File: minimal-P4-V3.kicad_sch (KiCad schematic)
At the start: 49 parts, among them U1 TLV62569DBV, U3 W25Q128JVS, Y1 40MHz(+-10 ppm)

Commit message: Start work on layout
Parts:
- C1, C12, C13, C15, C16, C17, C18, C19, C2, C21, C22, C23, C24, C25, C26, C27, C29, C30, C31, C32, C33, C4, C40, C41, C42, C5, C6, C7, C8, C9: footprint (none) -> Capacitor_SMD:C_0402_1005Metric
- C11, C14, C20, C28, C3: footprint (none) -> Capacitor_SMD:C_0603_1608Metric
- L1: footprint (none) -> Inductor_SMD:L_1008_2520Metric
- R1, R2, R200, R209, R210, R28, R3, R39, R4: footprint (none) -> Resistor_SMD:R_0402_1005Metric
- U2: footprint PCM_Espressif:ESP32-P4 -> Espressif:ESP32-P4
- Y1: value 40MHz(+-10 ppm) -> 40MHz(+-10 ppm) C501798; footprint (none) -> Crystal:Crystal_SMD_2016-4Pin_2.0x1.6mm
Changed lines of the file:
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@@
 			)
 		)
-		(property "Footprint" ""
+		(property "Footprint" "Capacitor_SMD:C_0402_1005Metric"
 			(at 140.97 186.69 0)
 			(hide yes)
@@
 			)
 		)
-		(property "Footprint" ""
+		(property "Footprint" "Capacitor_SMD:C_0402_1005Metric"
 			(at 231.14 41.91 0)
 			(hide yes)
@@
 			)
 		)
-		(property "Footprint" ""
+		(property "Footprint" "Capacitor_SMD:C_0402_1005Metric"
 			(at 220.98 71.12 0)
 			(hide yes)
@@
 			)
 		)
-		(property "Footprint" ""
+		(property "Footprint" "Resistor_SMD:R_0402_1005Metric"
 			(at 270.51 115.57 0)
 			(hide yes)
@@
 			)
 		)
-		(property "Footprint" ""
+		(property "Footprint" "Capacitor_SMD:C_0402_1005Metric"
 			(at 140.97 48.26 0)
 			(hide yes)
@@
 			)
 		)
-		(property "Footprint" ""
+		(property "Footprint" "Capacitor_SMD:C_0603_1608Metric"
 			(at 27.94 107.95 0)
 			(hide yes)
@@
 			)
 		)
-		(property "Footprint" ""
+		(property "Footprint" "Capacitor_SMD:C_0402_1005Metric"
 			(at 196.85 71.12 0)
 			(hide yes)
@@
 			)
 		)
-		(property "Footprint" ""
+		(property "Footprint" "Inductor_SMD:L_1008_2520Metric"
 			(at 213.36 39.37 0)
 			(hide yes)
@@
 			)
 		)
-		(property "Footprint" ""
+		(property "Footprint" "Resistor_SMD:R_0402_1005Metric"
 			(at 222.25 41.91 0)
 			(hide yes)
@@
 			)
 		)
-		(property "Footprint" ""
+		(property "Footprint" "Capacitor_SMD:C_0402_1005Metric"
 			(at 38.1 107.95 0)
 			(hide yes)
@@
 			)
 		)
-		(property "Footprint" ""
+		(property "Footprint" "Capacitor_SMD:C_0402_1005Metric"
 			(at 149.86 186.69 0)
 			(hide yes)
@@
 			)
 		)
-		(property "Footprint" ""
+		(property "Footprint" "Resistor_SMD:R_0402_1005Metric"
 			(at 278.13 115.57 0)
 			(hide yes)
@@
 			)
 		)
-		(property "Footprint" ""
+		(property "Footprint" "Capacitor_SMD:C_0402_1005Metric"
 			(at 53.34 165.1 0)
 			(hide yes)
@@
 			)
 		)
-		(property "Footprint" ""
+		(property "Footprint" "Capacitor_SMD:C_0402_1005Metric"
 			(at 237.49 71.12 0)
 			(hide yes)
@@
 			)
 		)
-		(property "Footprint" ""
+		(property "Footprint" "Capacitor_SMD:C_0402_1005Metric"
 			(at 232.41 104.14 0)
 			(hide yes)
@@
 			)
 		)
-		(property "Footprint" ""
+		(property "Footprint" "Resistor_SMD:R_0402_1005Metric"
 			(at 101.6 54.61 0)
 			(hide yes)
@@
 			)
 		)
-		(property "Footprint" ""
+		(property "Footprint" "Capacitor_SMD:C_0402_1005Metric"
 			(at 179.07 44.45 0)
 			(hide yes)
@@
 			)
 		)
-		(property "Footprint" ""
+		(property "Footprint" "Capacitor_SMD:C_0603_1608Metric"
 			(at 35.56 151.13 0)
 			(hide yes)
@@
 			)
 		)
-		(property "Footprint" ""
+		(property "Footprint" "Capacitor_SMD:C_0402_1005Metric"
 			(at 213.36 104.14 0)
 			(hide yes)
@@
 			)
 		)
-		(property "Footprint" ""
+		(property "Footprint" "Capacitor_SMD:C_0603_1608Metric"
 			(at 246.38 41.91 0)
 			(hide yes)
@@
 			)
 		)
-		(property "Footprint" ""
+		(property "Footprint" "Capacitor_SMD:C_0402_1005Metric"
 			(at 205.74 134.62 0)
 			(hide yes)
@@
 			)
 		)
-		(property "Footprint" ""
+		(property "Footprint" "Capacitor_SMD:C_0603_1608Metric"
 			(at 207.01 71.12 0)
 			(hide yes)
@@
 			)
 		)
-		(property "Footprint" ""
+		(property "Footprint" "Capacitor_SMD:C_0402_1005Metric"
 			(at 215.9 147.32 0)
 			(hide yes)
@@
 			)
 		)
-		(property "Footprint" ""
+		(property "Footprint" "Resistor_SMD:R_0402_1005Metric"
 			(at 57.15 62.23 0)
 			(hide yes)
@@
 			)
 		)
-		(property "Footprint" ""
+		(property "Footprint" "Capacitor_SMD:C_0402_1005Metric"
 			(at 74.93 52.07 0)
 			(hide yes)
@@
 			)
 		)
-		(property "Footprint" ""
+		(property "Footprint" "Capacitor_SMD:C_0402_1005Metric"
 			(at 38.1 138.43 0)
 			(hide yes)
@@
 			)
 		)
-		(property "Footprint" ""
+		(property "Footprint" "Capacitor_SMD:C_0402_1005Metric"
 			(at 242.57 104.14 0)
 			(hide yes)
@@
 			)
 		)
-		(property "Footprint" ""
+		(property "Footprint" "Capacitor_SMD:C_0402_1005Metric"
 			(at 96.52 177.8 0)
 			(hide yes)
@@
 			)
 		)
-		(property "Footprint" ""
+		(property "Footprint" "Resistor_SMD:R_0402_1005Metric"
 			(at 226.06 144.78 0)
 			(hide yes)
@@
 			)
 		)
-		(property "Footprint" ""
+		(property "Footprint" "Capacitor_SMD:C_0402_1005Metric"
 			(at 105.41 39.37 0)
 			(hide yes)
@@
 			)
 		)
-		(property "Footprint" ""
+		(property "Footprint" "Capacitor_SMD:C_0402_1005Metric"
 			(at 114.3 48.26 0)
 			(hide yes)
@@
 			)
 		)
-		(property "Footprint" ""
+		(property "Footprint" "Capacitor_SMD:C_0402_1005Metric"
 			(at 95.25 39.37 0)
 			(hide yes)
@@
 			)
 		)
-		(property "Footprint" ""
+		(property "Footprint" "Capacitor_SMD:C_0402_1005Metric"
 			(at 222.25 104.14 0)
 			(hide yes)
@@
 			)
 		)
-		(property "Footprint" ""
+		(property "Footprint" "Capacitor_SMD:C_0402_1005Metric"
 			(at 160.02 186.69 0)
 			(hide yes)
@@
 			)
 		)
-		(property "Footprint" "PCM_Espressif:ESP32-P4"
+		(property "Footprint" "Espressif:ESP32-P4"
 			(at 66.04 158.75 0)
 			(hide yes)
@@
 			)
 		)
-		(property "Footprint" ""
+		(property "Footprint" "Capacitor_SMD:C_0603_1608Metric"
 			(at 64.77 52.07 0)
 			(hide yes)
@@
 			)
 		)
-		(property "Footprint" ""
+		(property "Footprint" "Resistor_SMD:R_0402_1005Metric"
 			(at 222.25 49.53 0)
 			(hide yes)
@@
 			)
 		)
-		(property "Footprint" ""
+		(property "Footprint" "Capacitor_SMD:C_0402_1005Metric"
 			(at 127 48.26 0)
 			(hide yes)
@@
 			)
 		)
-		(property "Value" "40MHz(+-10 ppm)"
+		(property "Value" "40MHz(+-10 ppm) C501798"
 			(at 100.33 29.972 0)
 			(show_name no)
@@
 			)
 		)
-		(property "Footprint" ""
+		(property "Footprint" "Crystal:Crystal_SMD_2016-4Pin_2.0x1.6mm"
 			(at 100.33 39.37 0)
 			(hide yes)
@@
 			)
 		)
-		(property "Footprint" ""
+		(property "Footprint" "Capacitor_SMD:C_0402_1005Metric"
 			(at 229.87 127 0)
 			(hide yes)
@@
 			)
 		)
-		(property "Footprint" ""
+		(property "Footprint" "Capacitor_SMD:C_0402_1005Metric"
 			(at 57.15 69.85 0)
 			(hide yes)
@@
 			)
 		)
-		(property "Footprint" ""
+		(property "Footprint" "Capacitor_SMD:C_0402_1005Metric"
 			(at 87.63 177.8 0)
 			(hide yes)
@@
 			)
 		)
-		(property "Footprint" ""
+		(property "Footprint" "Capacitor_SMD:C_0402_1005Metric"
 			(at 80.01 39.37 0)
 			(hide yes)
@@
 			)
 		)
-		(property "Footprint" ""
+		(property "Footprint" "Resistor_SMD:R_0402_1005Metric"
 			(at 99.06 54.61 0)
 			(hide yes)
@@
 			)
 		)
-		(property "Footprint" ""
+		(property "Footprint" "Capacitor_SMD:C_0402_1005Metric"
 			(at 44.45 151.13 0)
 			(hide yes)
@@
 			)
 		)
-		(property "Footprint" ""
+		(property "Footprint" "Resistor_SMD:R_0402_1005Metric"
 			(at 36.83 165.1 0)
 			(hide yes)
@@
 			)
 		)
-		(property "Footprint" ""
+		(property "Footprint" "Capacitor_SMD:C_0402_1005Metric"
 			(at 217.17 134.62 0)
 			(hide yes)

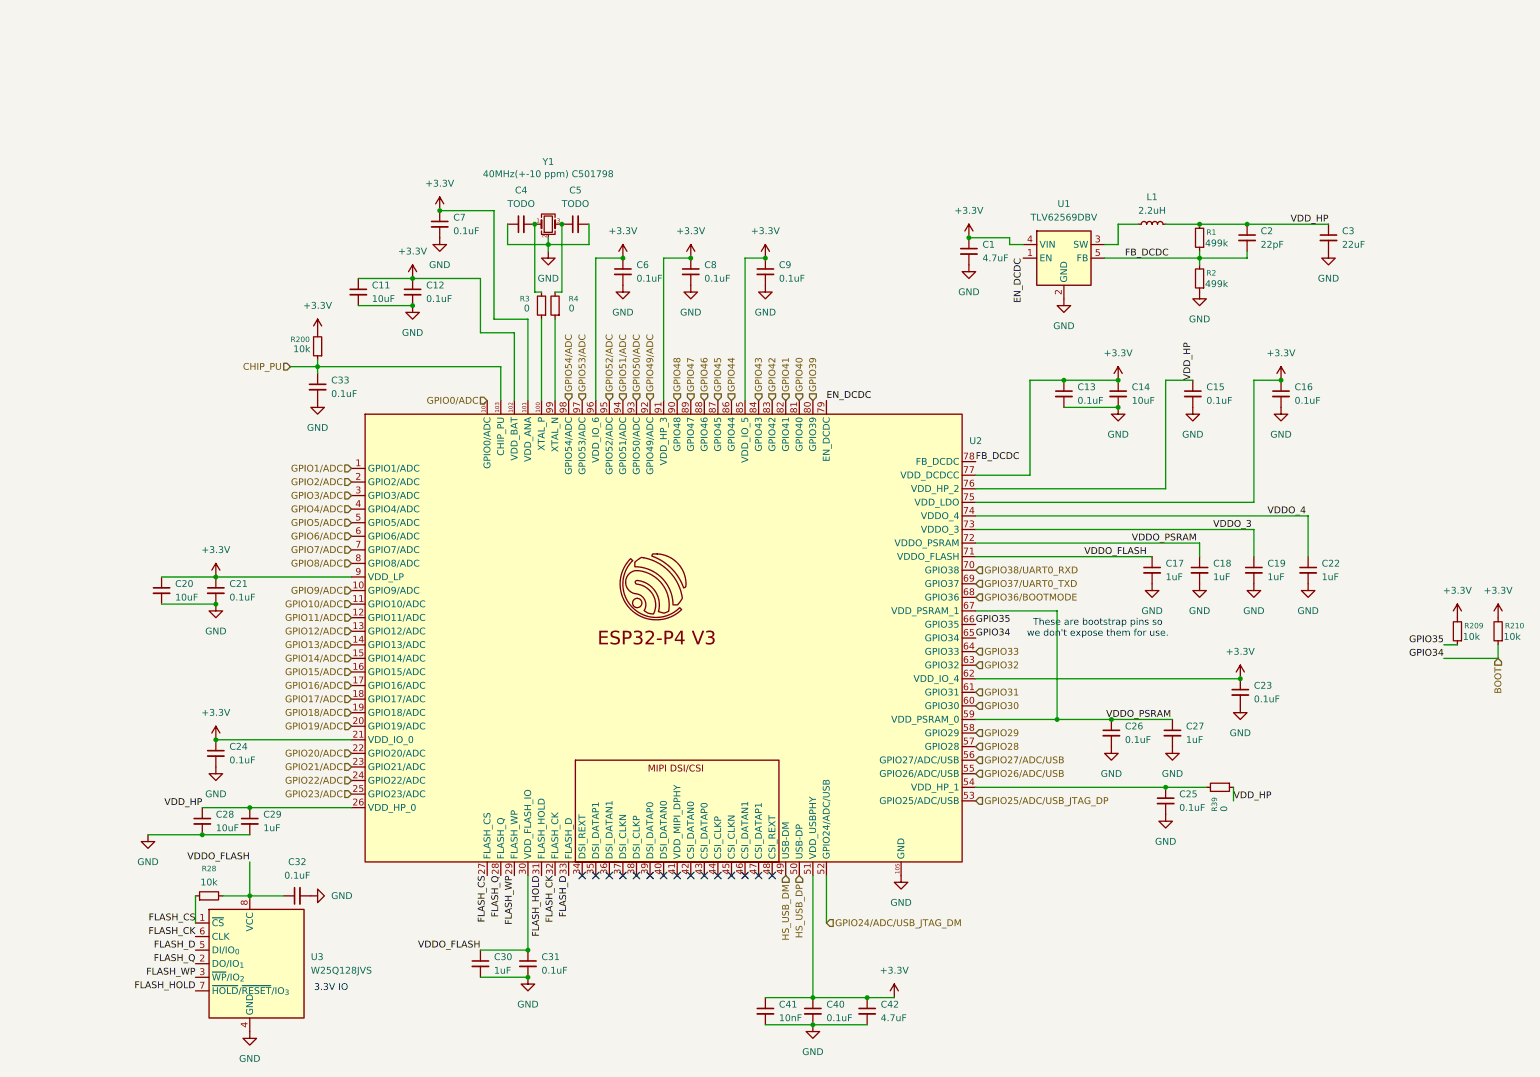
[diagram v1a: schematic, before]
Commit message: Setup design rules. Start to match up pins
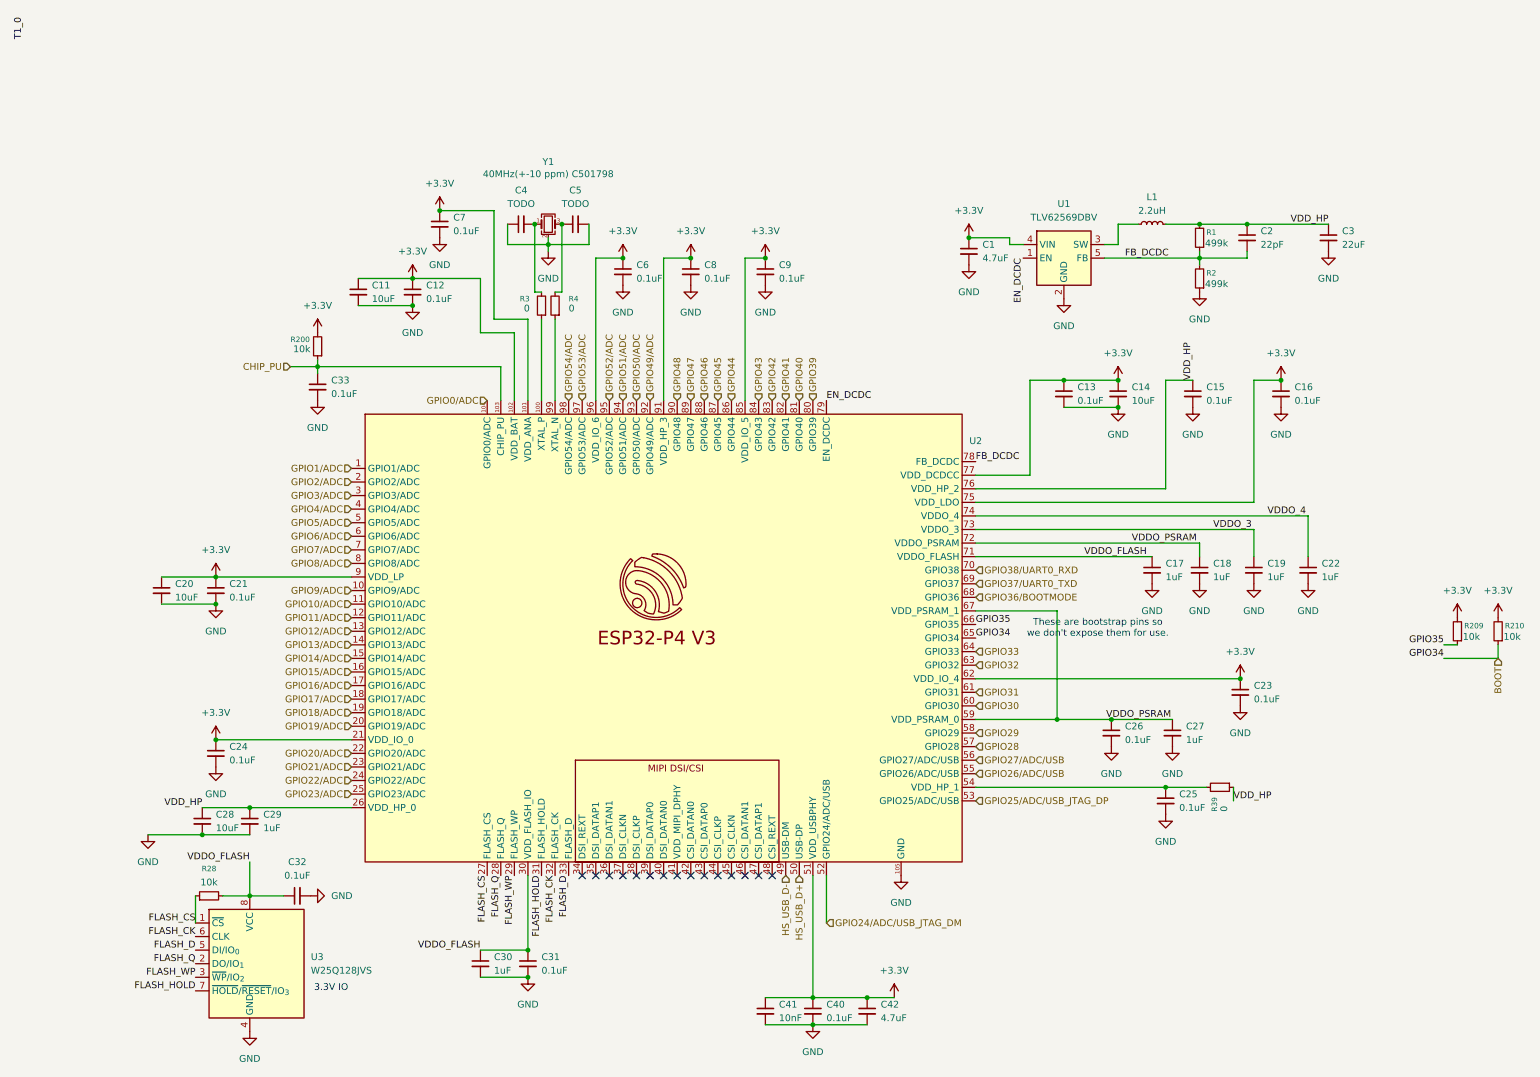
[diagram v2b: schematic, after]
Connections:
- net HS_USB_DM renamed HS_USB_D-
- net HS_USB_DP renamed HS_USB_D+

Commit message: Lots more routing and placement
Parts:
- removed C19, C22: 1uF, Capacitor_SMD:C_0402_1005Metric, symbol Device:C_Small
- U3: footprint Package_SO:SOIC-8_5.3x5.3mm_P1.27mm -> Package_SON:WSON-8-1EP_6x5mm_P1.27mm_EP3.4x4.3mm
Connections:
- net +3.3V: no longer C8.1, U2.91 (VDD_HP_3)
- net VDDO_FLASH: no longer C30.1, C31.1, C32.1, R28.2, U2.30 (VDD_FLASH_IO), U3.8 (VCC)
- net VDD_HP: now also C8.1, U2.91 (VDD_HP_3)
- net VDDO_3: no longer names the net of U2.73 (VDDO_3)
- net VDDO_4: no longer names the net of U2.74 (VDDO_4)
- new net VDD_FLASH: C30.1, C31.1, C32.1, R28.2, U2.30 (VDD_FLASH_IO), U3.8 (VCC)
- no-connect marks 15 -> 17

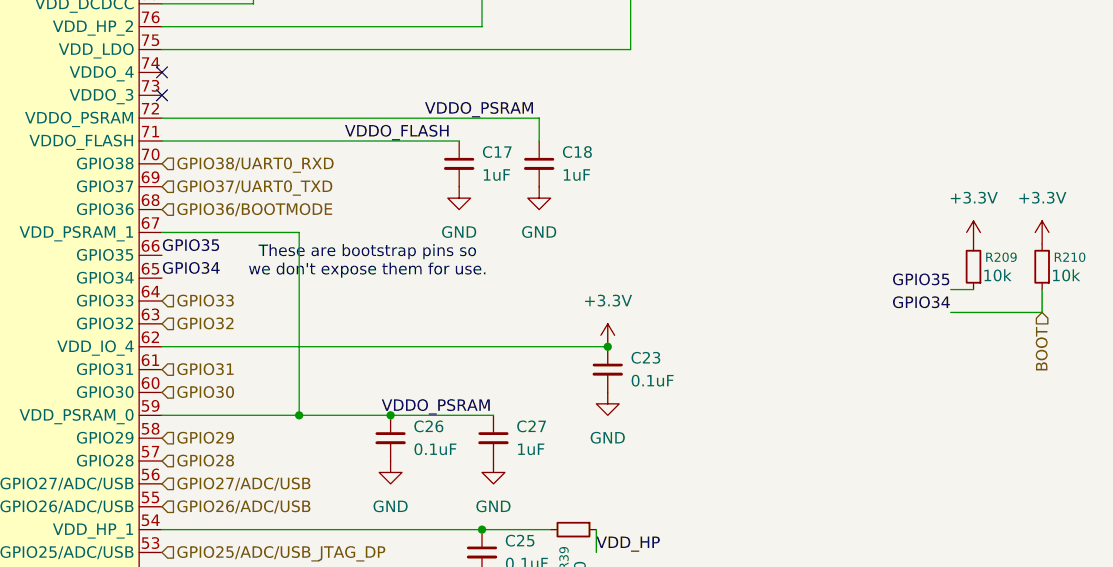
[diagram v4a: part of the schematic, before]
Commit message: Fix bootstrapping pins. Start fixing DRC
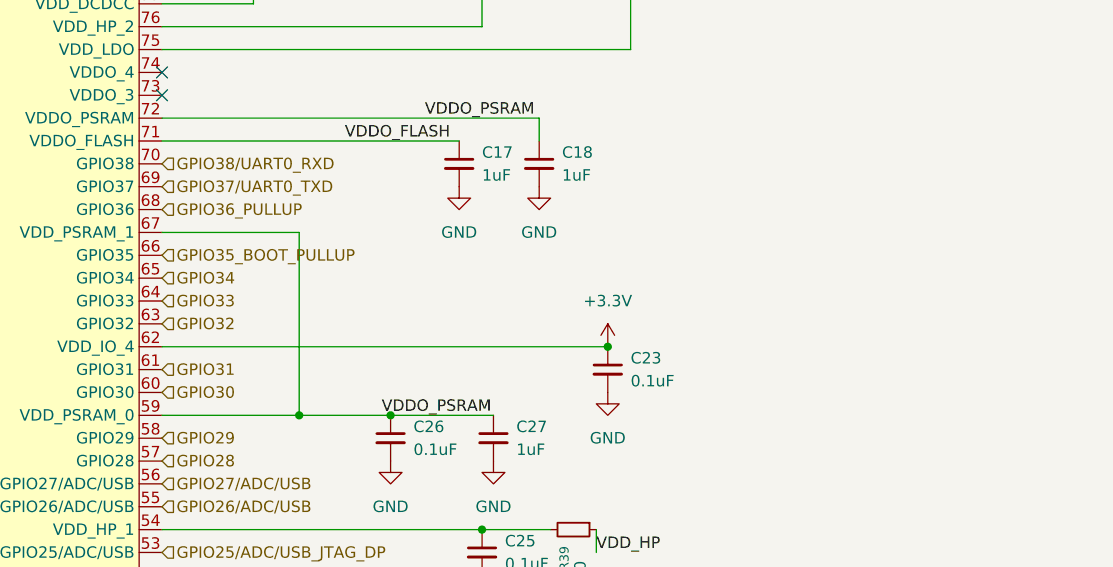
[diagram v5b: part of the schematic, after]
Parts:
- removed R209, R210: 10k, Resistor_SMD:R_0402_1005Metric, symbol Device:R_Small
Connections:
- net BOOT renamed GPIO34
- net GPIO35 renamed GPIO35_BOOT_PULLUP
- net GPIO36/BOOTMODE renamed GPIO36_PULLUP
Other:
- note removed: "These are bootstrap pins so we don't expose them for use."

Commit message: Done?
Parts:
- C4, C5: value TODO -> 12pF
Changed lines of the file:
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@@
 			)
 		)
-		(property "Value" "TODO"
+		(property "Value" "12pF"
 			(at 105.4163 35.56 90)
 			(show_name no)
@@
 			)
 		)
-		(property "Value" "TODO"
+		(property "Value" "12pF"
 			(at 95.2563 35.56 90)
 			(show_name no)

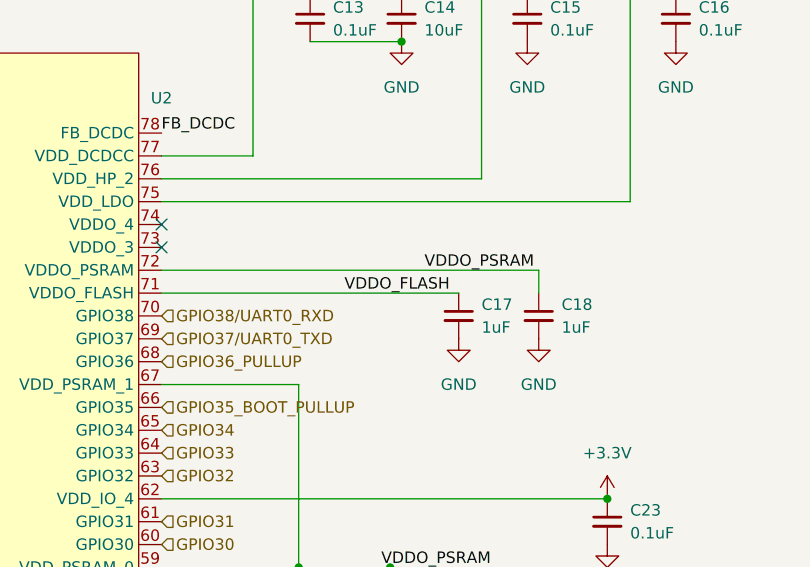
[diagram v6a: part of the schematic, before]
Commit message: Connect flash VDD and skooch USBs apart. Start of v2
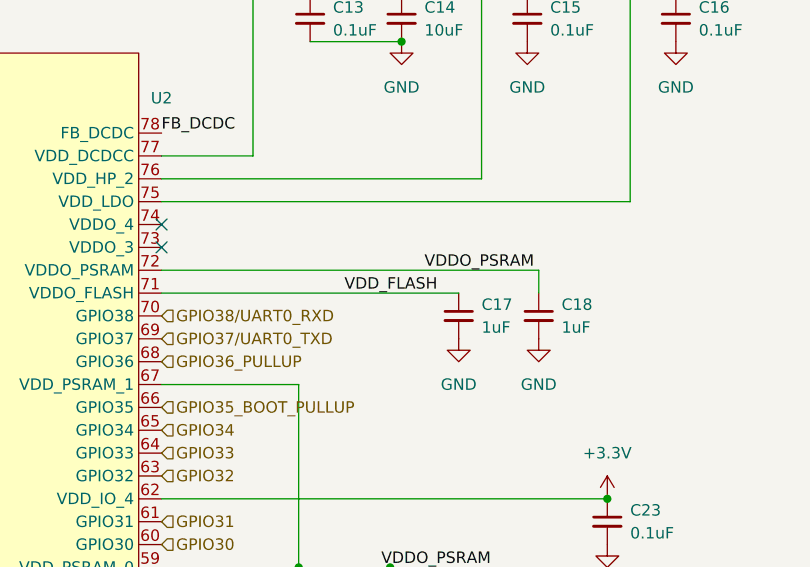
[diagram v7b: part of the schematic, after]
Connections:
- net VDDO_FLASH is gone; now on net VDD_FLASH: C17.1, U2.71 (VDDO_FLASH)
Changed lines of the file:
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@@
 		)
 	)
-	(label "VDDO_FLASH"
+	(label "VDD_FLASH"
 		(at 200.66 101.6 0)
 		(effects
@@
 	)
 	(group "Minimal P4"
+		(members "fa4e65ae-e387-4699-8943-9df01c62cf29")
+	)
+	(group "Minimal P4 V3"
+		(lib_id "Espressif:Minimal P4 V3")
 		(members "008b715d-e8da-4df3-8723-02ccdaa80df5" "01d0c653-ddd9-4bb7-a9d1-9bd4facf6944"
 			"01d56d51-753a-4c1f-8696-b241f55c7d35" "02945611-2a84-4ce7-a537-efee910da38f"

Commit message: ready for v2
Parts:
- C17, C18, C27, C29, C30: value 1uF -> 1uF/16V(10%)
- R200, R28: value 10k -> 10K(1%)
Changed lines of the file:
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@@
 			)
 		)
-		(property "Value" "1uF"
+		(property "Value" "1uF/16V(10%)"
 			(at 215.9 105.4162 0)
 			(show_name no)
@@
 			)
 		)
-		(property "Value" "10k"
+		(property "Value" "10K(1%)"
 			(at 52.578 62.738 0)
 			(show_name no)
@@
 			)
 		)
-		(property "Value" "1uF"
+		(property "Value" "1uF/16V(10%)"
 			(at 224.79 105.4162 0)
 			(show_name no)
@@
 			)
 		)
-		(property "Value" "1uF"
+		(property "Value" "1uF/16V(10%)"
 			(at 90.17 179.0762 0)
 			(show_name no)
@@
 			)
 		)
-		(property "Value" "1uF"
+		(property "Value" "1uF/16V(10%)"
 			(at 46.99 152.4062 0)
 			(show_name no)
@@
 			)
 		)
-		(property "Value" "10k"
+		(property "Value" "10K(1%)"
 			(at 36.83 162.56 90)
 			(show_name no)
@@
 			)
 		)
-		(property "Value" "1uF"
+		(property "Value" "1uF/16V(10%)"
 			(at 219.71 135.8962 0)
 			(show_name no)
